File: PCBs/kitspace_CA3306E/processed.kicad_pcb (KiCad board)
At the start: 2 copper layers, 65 x 30 mm, 10 parts

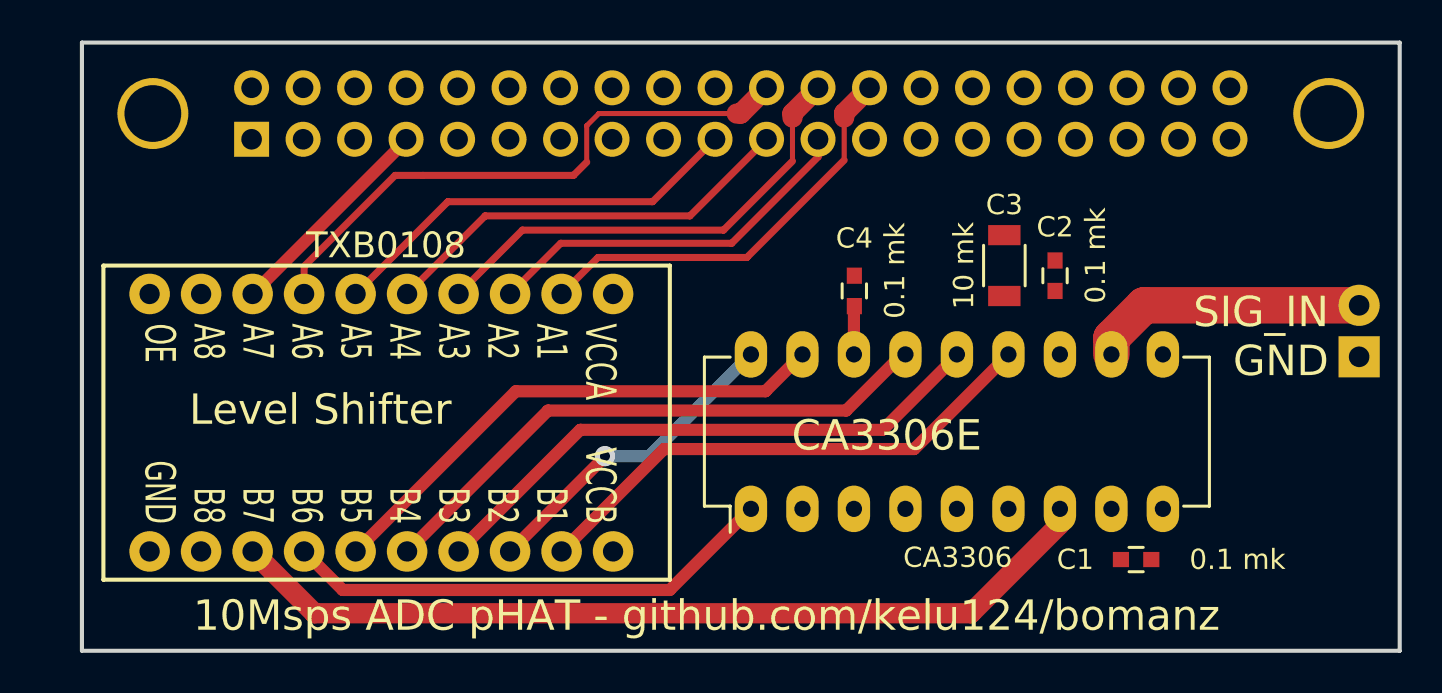
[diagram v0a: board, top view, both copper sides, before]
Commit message: recheck all circuits and clean up fill zone by rerouting the nets using freerouting and manually
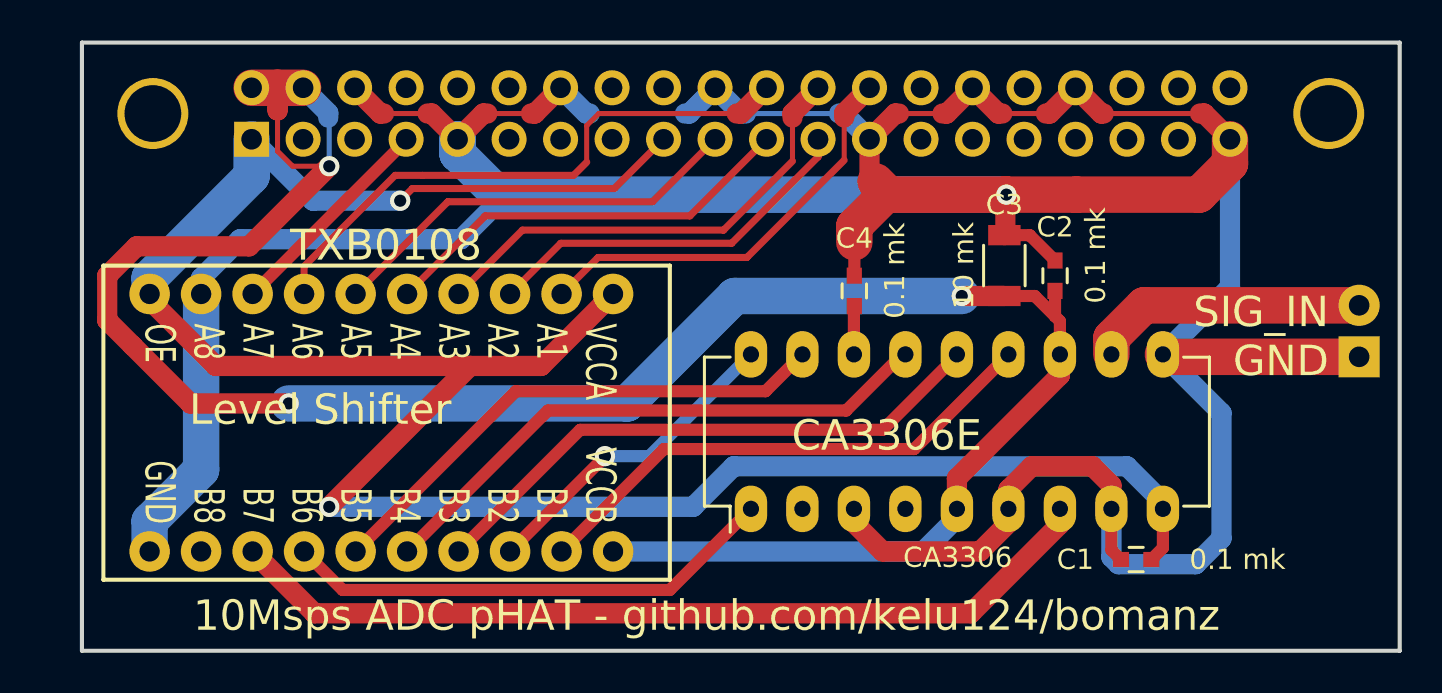
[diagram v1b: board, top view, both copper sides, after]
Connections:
- C1 pad 1: (no net) -> VDD_3V3
- C1 pad 2: (no net) -> GND
- C2 pad 1: (no net) -> VDD_5V
- C2 pad 2: (no net) -> GND
- C3 pad 1: (no net) -> VDD_5V
- C3 pad 2: (no net) -> GND
- C4 pad 2: (no net) -> GND
- CA3306 pad 10: (no net) -> GND
- CA3306 pad 12: (no net) -> VDD_5V
- CA3306 pad 3: (no net) -> GND
- CA3306 pad 5: (no net) -> VDD_5V
- CA3306 pad 6: (no net) -> GND
- CA3306 pad 8: (no net) -> GND
- CA3306 pad 9: (no net) -> VDD_3V3
- TXB0108 pad 1: (no net) -> VDD_3V3
- TXB0108 pad 10: (no net) -> VDD_3V3
- TXB0108 pad 11: (no net) -> GND
- TXB0108 pad 20: (no net) -> VDD_5V
- TXB0108 pad 9: (no net) -> GND
- XS1 pad 1: (no net) -> VDD_3V3
- XS1 pad 14: (no net) -> GND
- XS1 pad 17: (no net) -> VDD_3V3
- XS1 pad 2: (no net) -> VDD_5V
- XS1 pad 20: (no net) -> GND
- XS1 pad 25: (no net) -> GND
- XS1 pad 30: (no net) -> GND
- XS1 pad 34: (no net) -> GND
- XS1 pad 39: (no net) -> GND
- XS1 pad 4: (no net) -> VDD_5V
- XS1 pad 6: (no net) -> GND
- XS1 pad 9: (no net) -> GND
- XT1 pad 1: (no net) -> GND
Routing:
- net GND: track 0.00 -> 207.6 mm, vias 0 -> 1
- net VDD_3V3: track 0.00 -> 114.7 mm, vias 0 -> 2
- net VDD_5V: track 0.00 -> 110.7 mm, vias 0 -> 3

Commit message: clean psbc that are missed before
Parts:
- renumbered REF** to REF**_2
